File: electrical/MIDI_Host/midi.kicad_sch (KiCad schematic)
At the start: 25 parts, among them U1 BL1551B, U2 BL1551B, U3 BL1551B, U5 74HC1G14GV, U6 6N137, U7 6N137

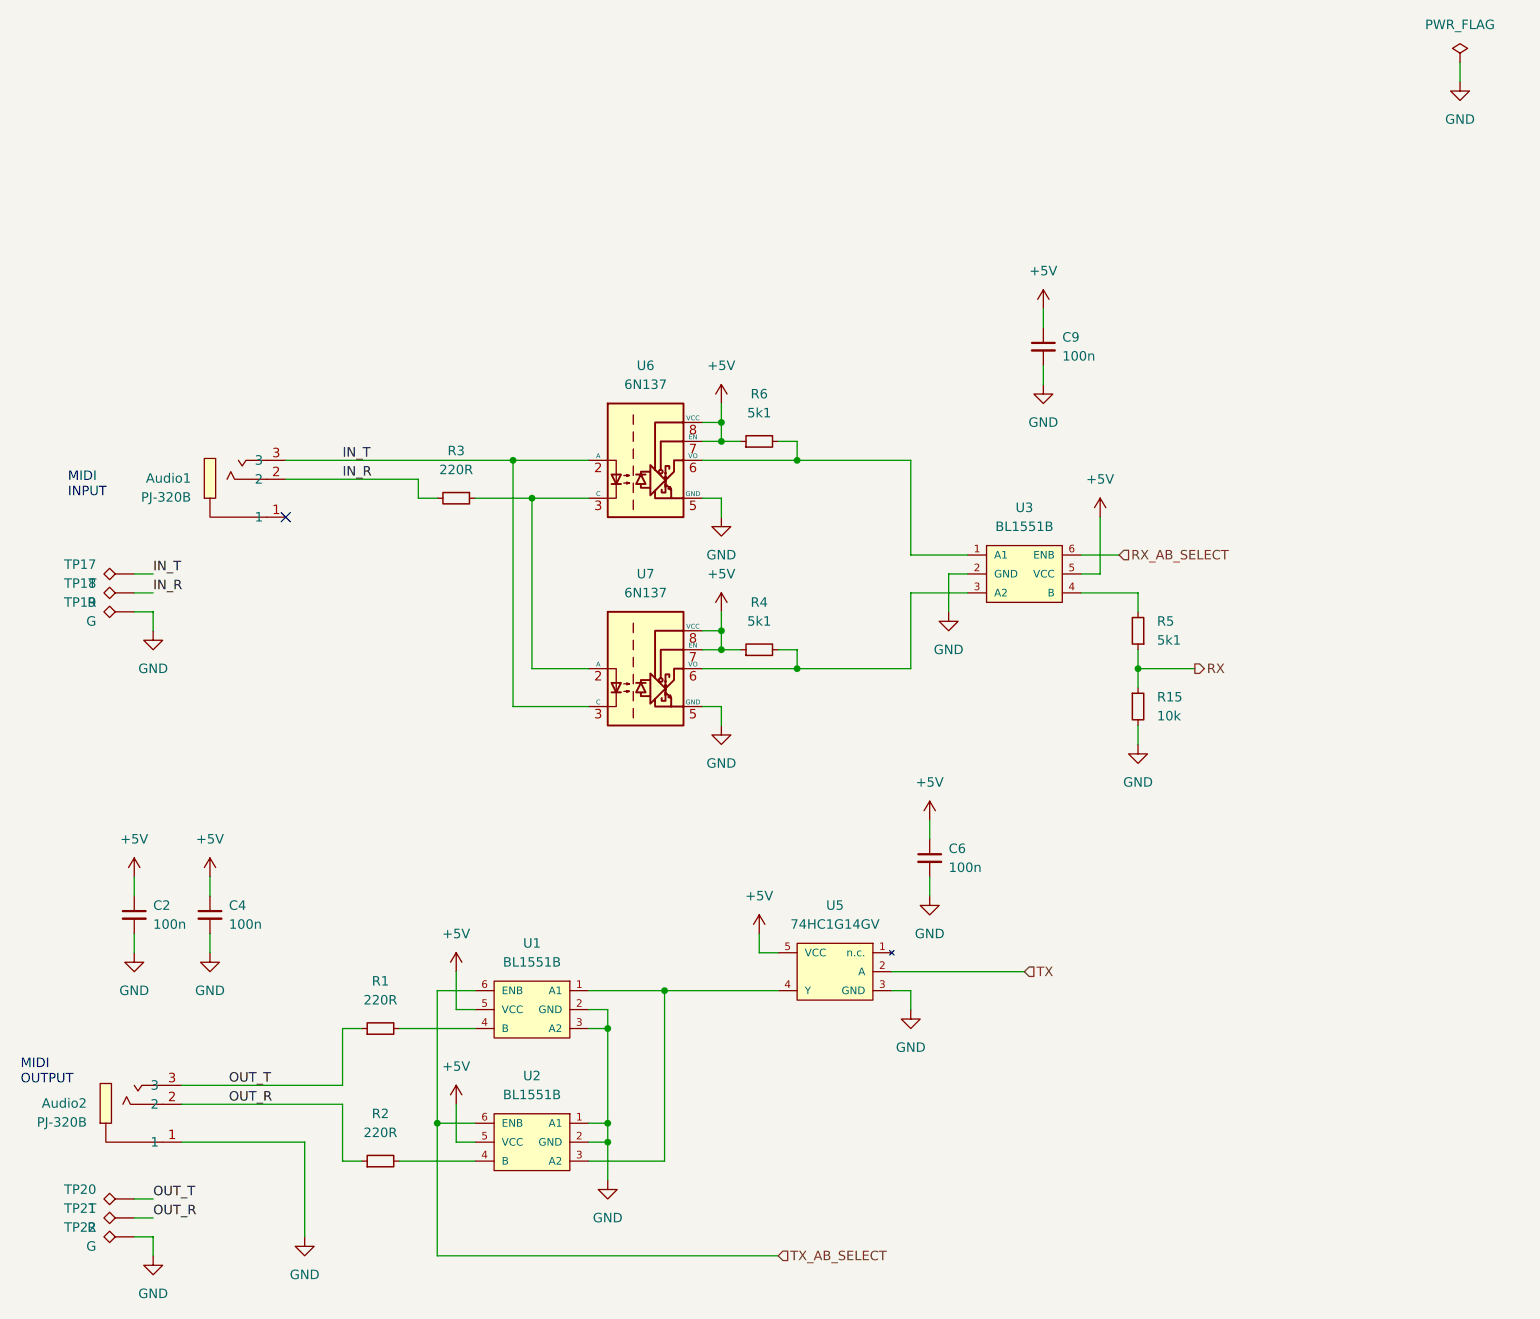
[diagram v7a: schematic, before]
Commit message: SUKU connectors moved back, gerber testpoint names fixed
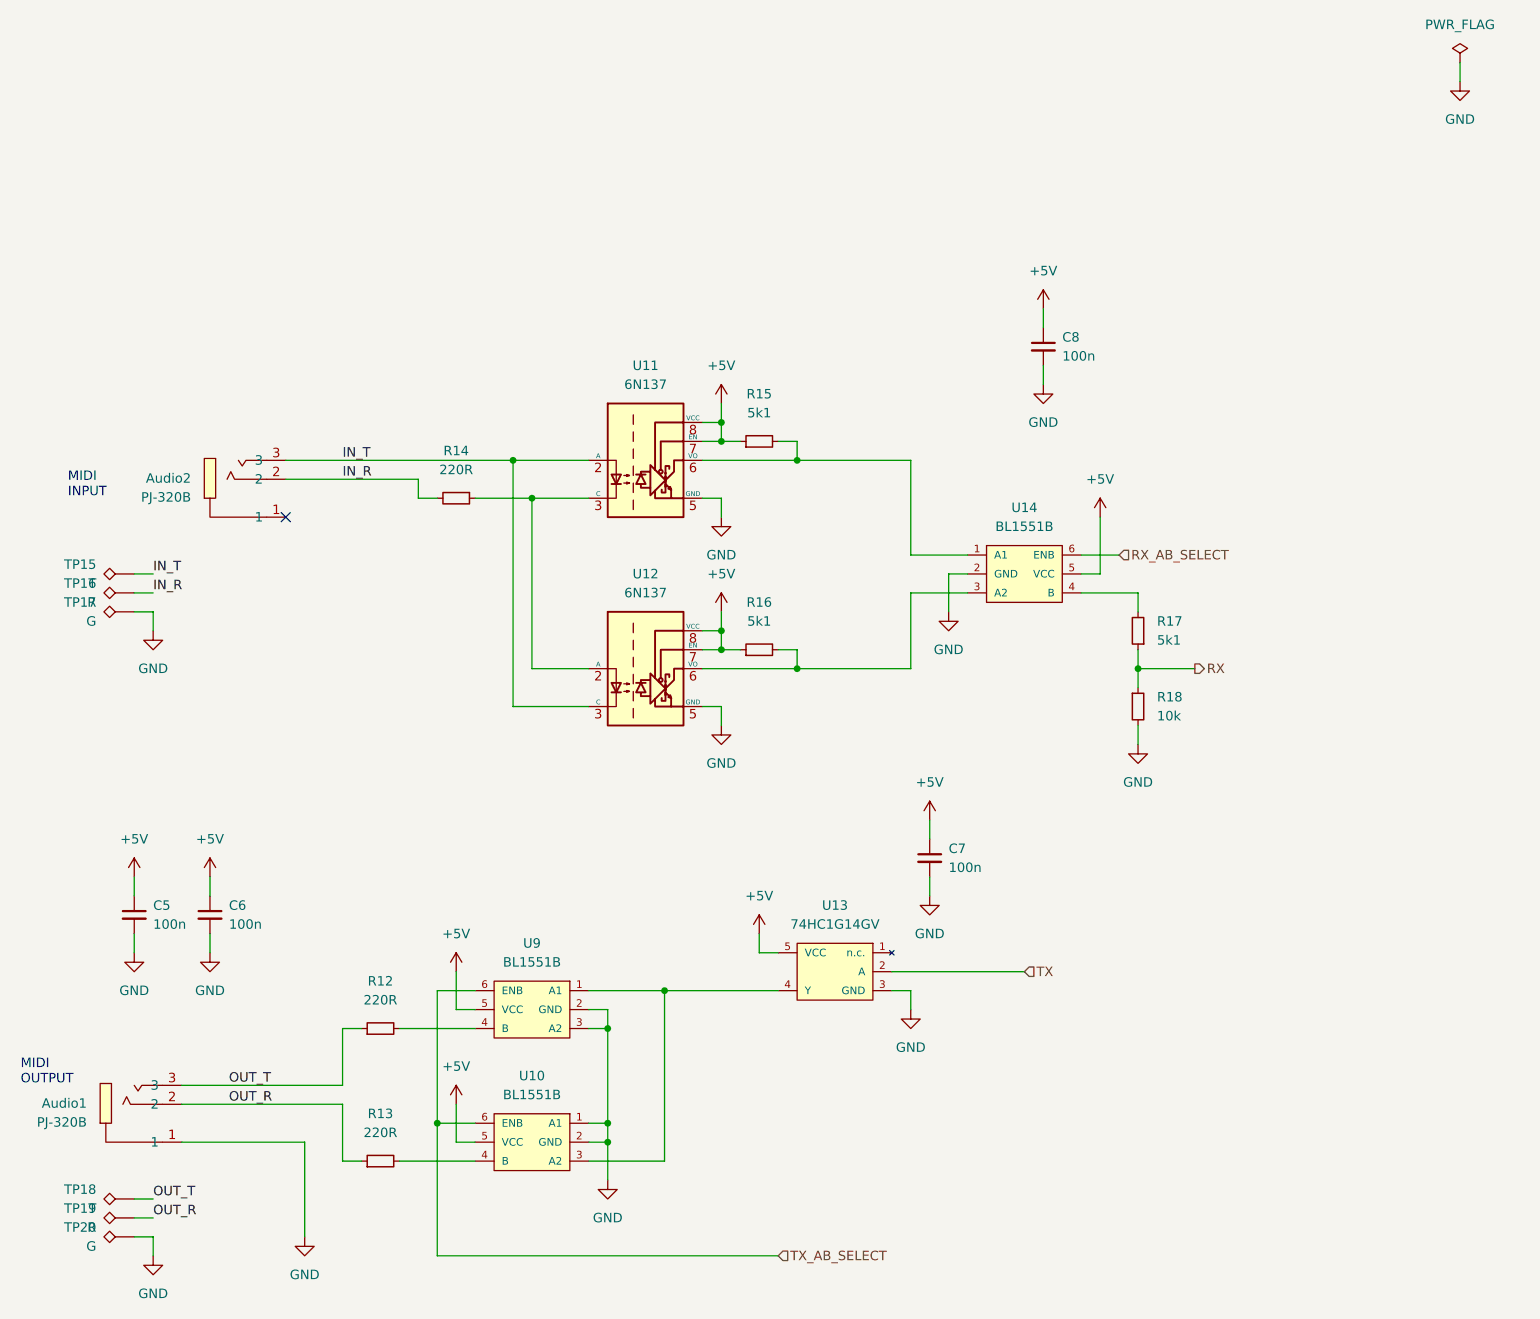
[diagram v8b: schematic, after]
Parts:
- renumbered Audio2 to Audio1, Audio1 to Audio2, C2 to C5, C4 to C6, C6 to C7, C9 to C8, R1 to R12, R2 to R13, R3 to R14, R6 to R15, R4 to R16, R5 to R17, R15 to R18, TP17 to TP15, TP18 to TP16, TP19 to TP17, TP20 to TP18, TP21 to TP19, TP22 to TP20, U2 to U10, U6 to U11, U7 to U12, U5 to U13, U3 to U14, U1 to U9
